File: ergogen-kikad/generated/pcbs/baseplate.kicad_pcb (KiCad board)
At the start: 2 copper layers, 73.6 x 60.5 mm, 13 parts

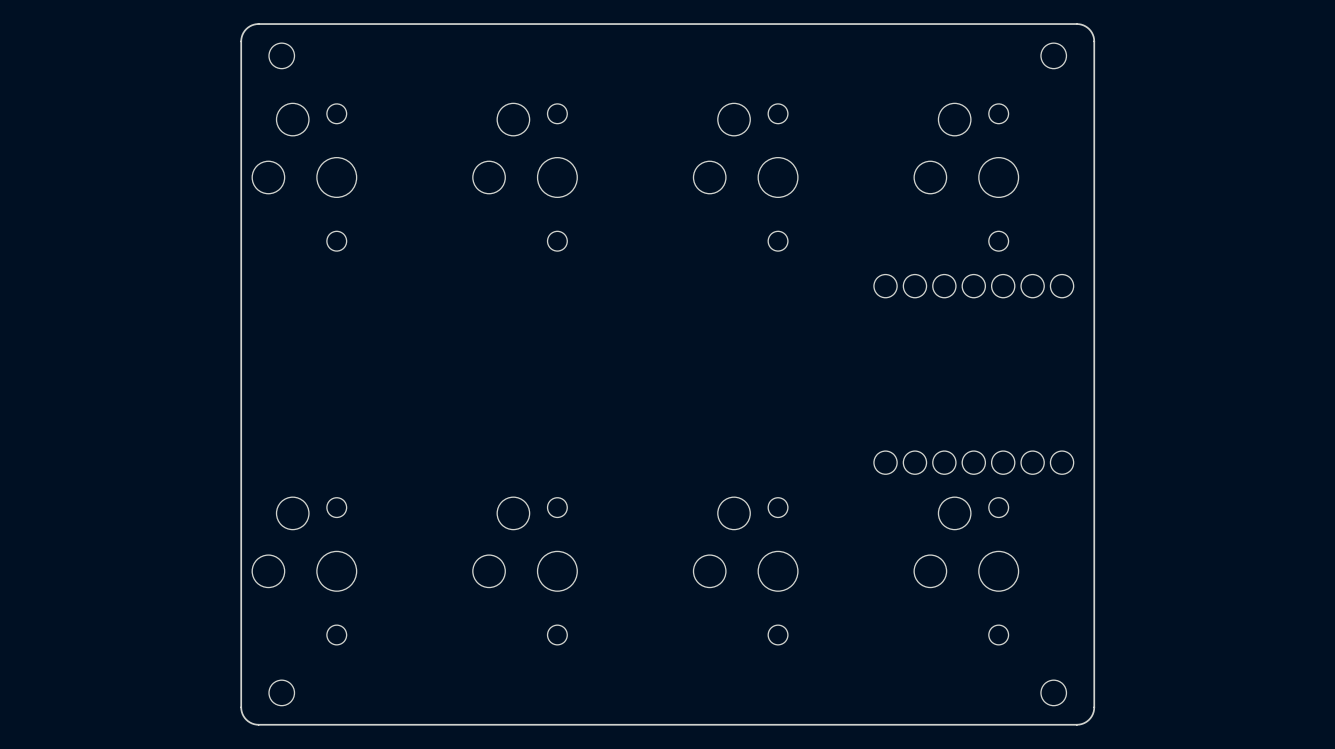
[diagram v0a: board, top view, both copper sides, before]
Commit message: Compact key rows and add controller-side keys through Ergogen
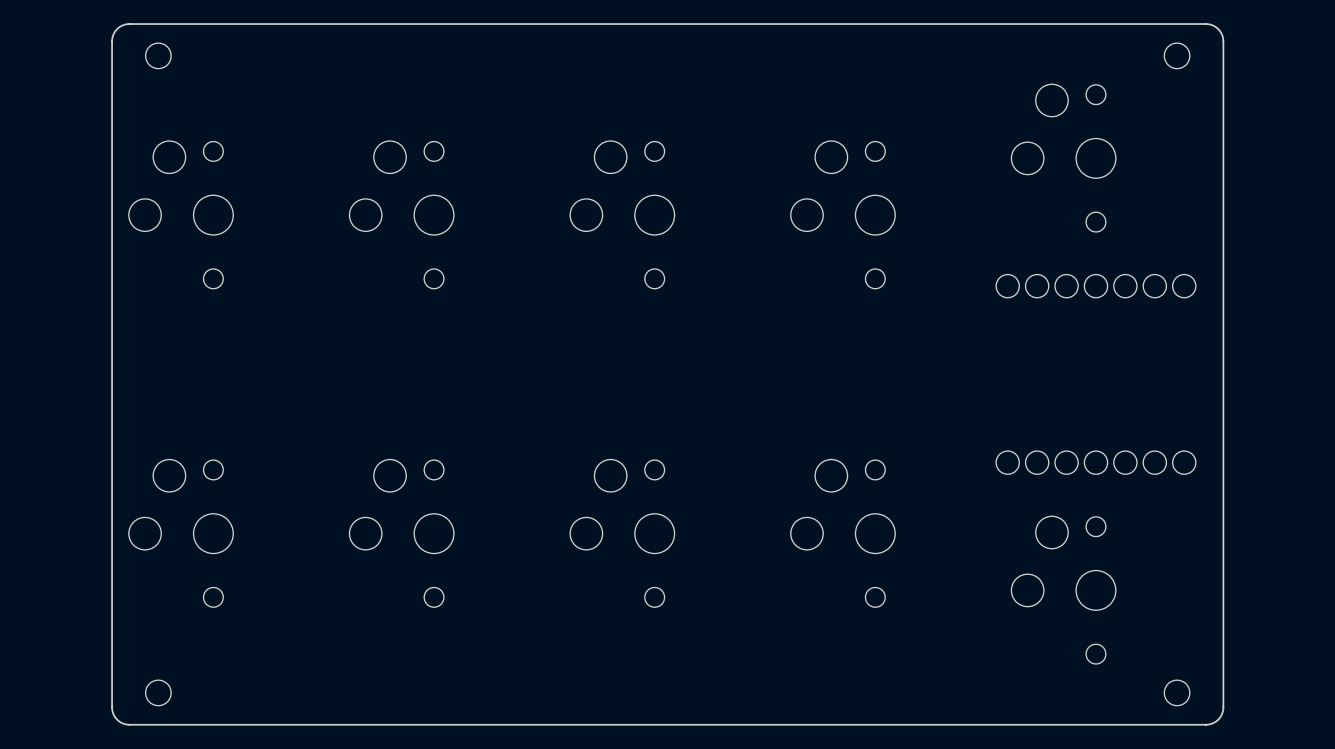
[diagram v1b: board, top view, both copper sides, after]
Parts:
- added S10: Choc v1 1U, PG1350_1U, F.Cu at (247.0, 167.2)
- added S9: Choc v1 1U, PG1350_1U, F.Cu at (247.0, 129.8)
- moved S1 11.1 mm to (170.8, 134.8)
- moved S2 11.1 mm to (189.8, 134.8)
- moved S3 11.1 mm to (208.9, 134.8)
- moved S5 11.1 mm to (170.8, 162.2)
- moved S6 11.1 mm to (189.8, 162.2)
- moved S7 11.1 mm to (208.9, 162.2)
- moved S4 11.1 mm to (227.9, 134.8)
- moved S8 11.1 mm to (227.9, 162.2)
- moved H1 10.7 mm to (166.0, 121.0)
- moved H2 10.7 mm to (254.0, 121.0)
- moved H3 10.7 mm to (166.0, 176.0)
- moved H4 10.7 mm to (254.0, 176.0)
- moved MCU1 10.5 mm to (247.0, 148.5)
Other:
- board size 73.6 x 60.5 mm -> 96 x 60.5 mm

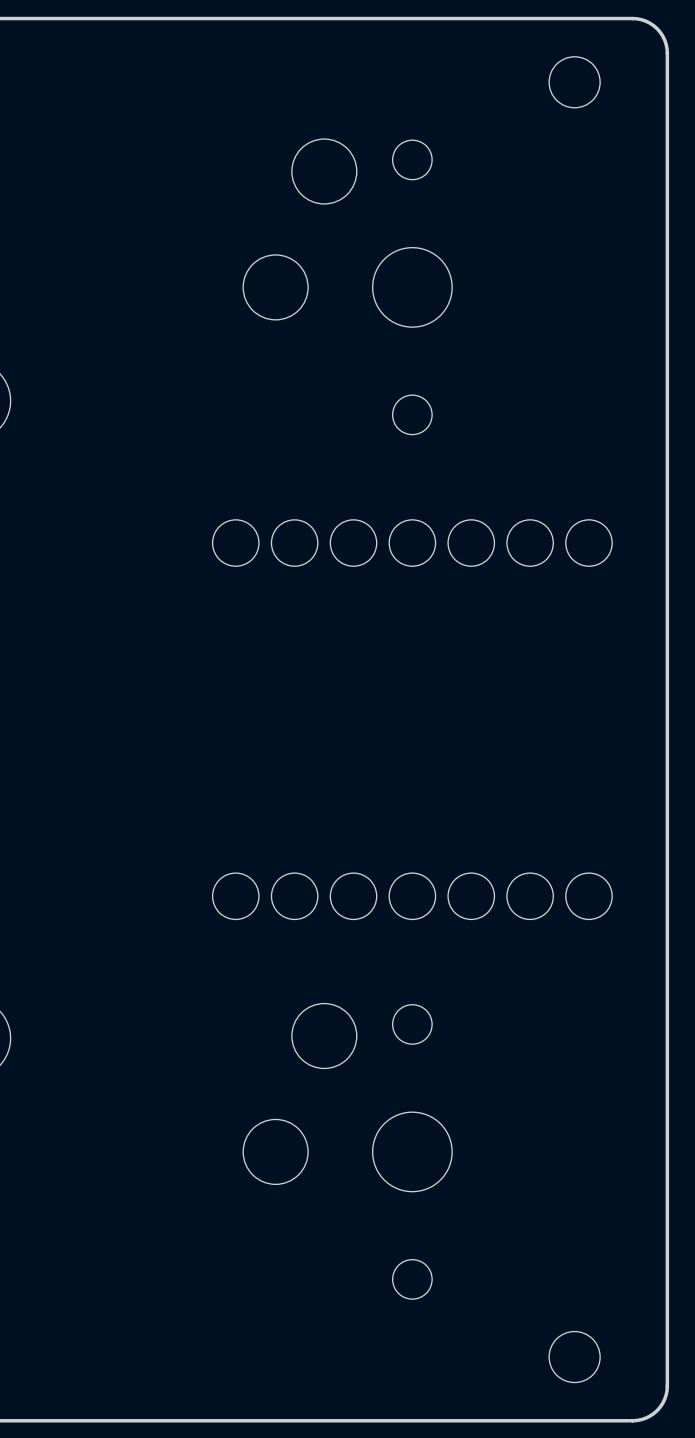
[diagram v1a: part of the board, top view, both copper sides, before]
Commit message: Align fifth-column caps with outer row edges
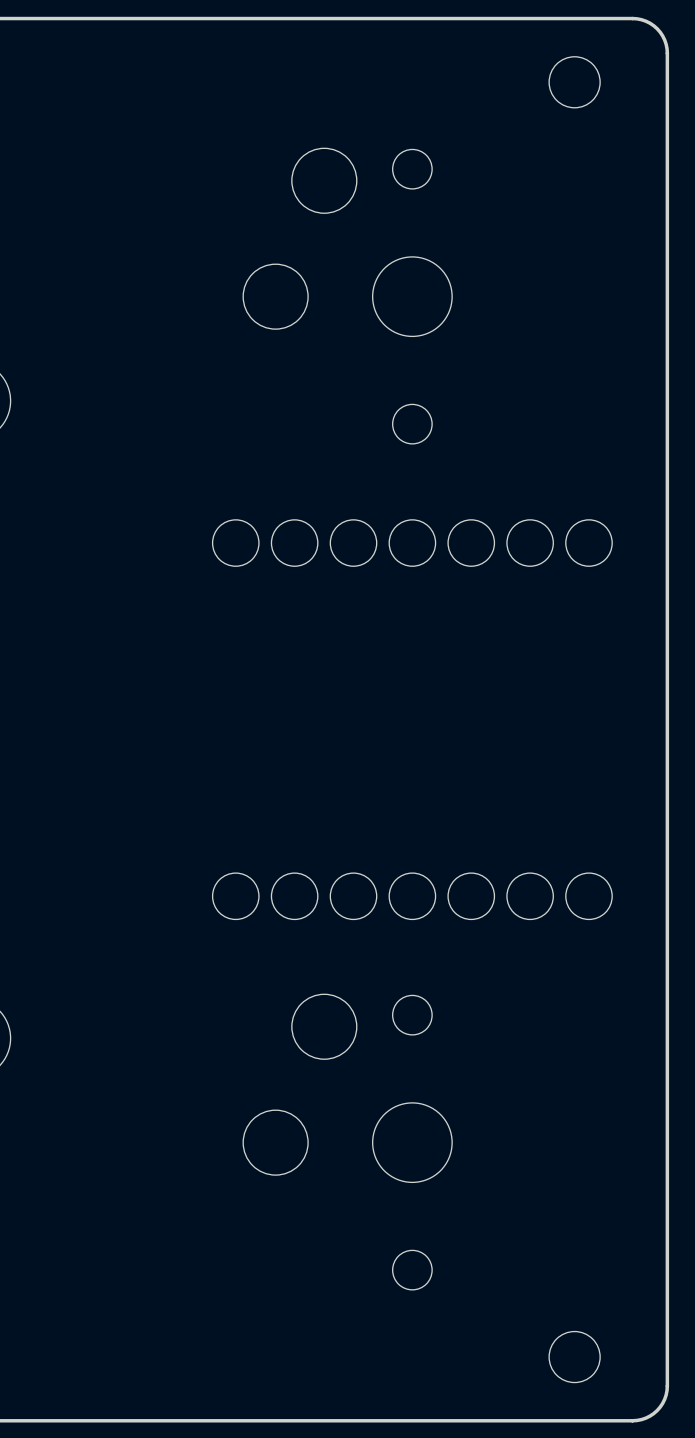
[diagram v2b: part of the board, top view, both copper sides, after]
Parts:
- moved S10 0.40 mm to (247.0, 166.8)
- moved S9 0.40 mm to (247.0, 130.2)

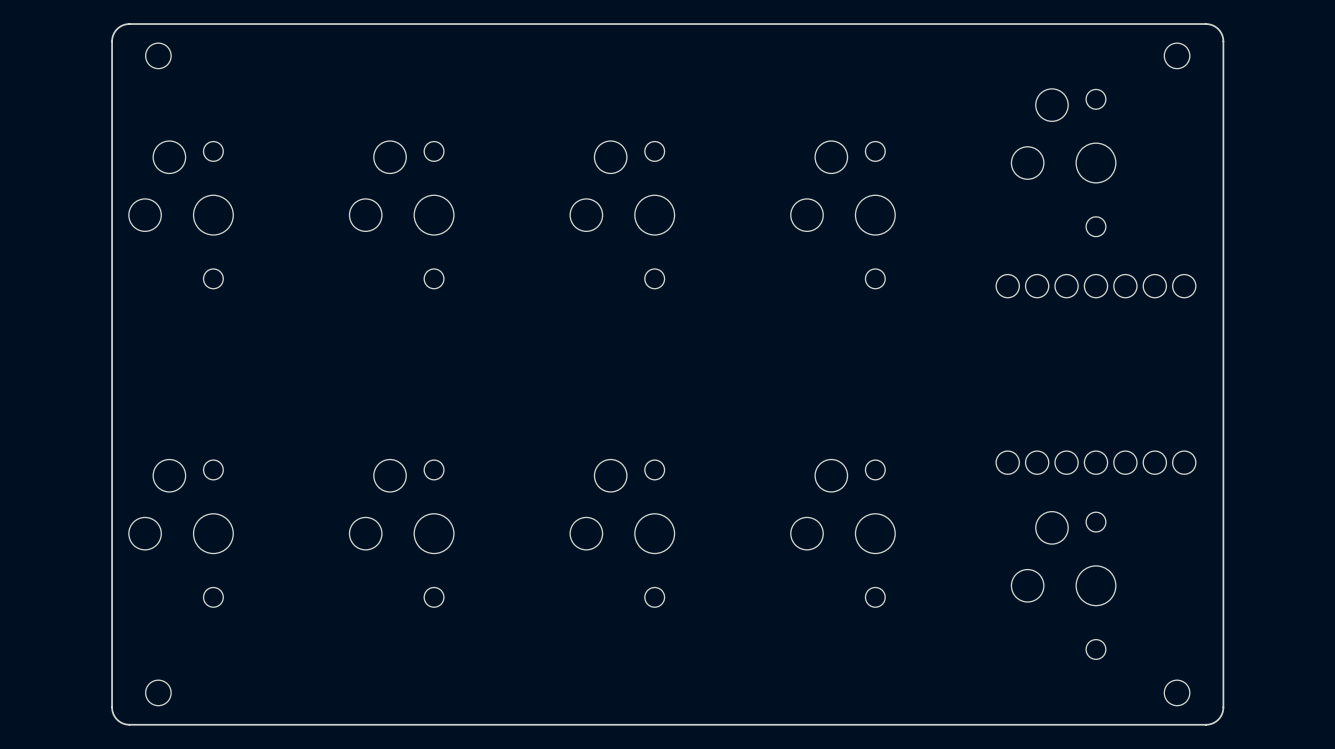
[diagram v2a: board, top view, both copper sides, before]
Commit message: Move mounts between switches and trim the board border
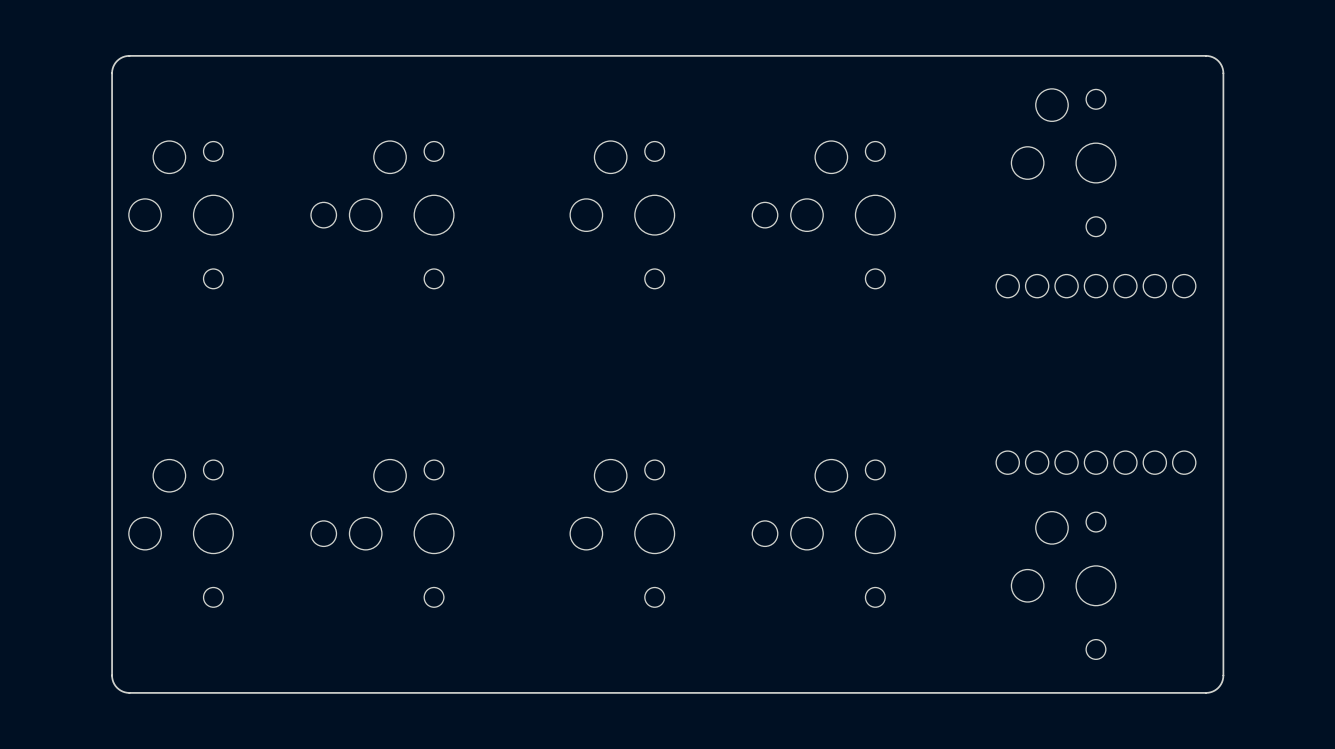
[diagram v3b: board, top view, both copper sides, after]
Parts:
- moved H2 38.1 mm to (218.4, 134.8)
- moved H4 38.1 mm to (218.4, 162.2)
- moved H1 19.8 mm to (180.3, 134.8)
- moved H3 19.8 mm to (180.3, 162.2)
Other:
- board size 96 x 60.5 mm -> 96 x 55 mm

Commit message: Add compact stacked memory LCD and regenerate matching carrier
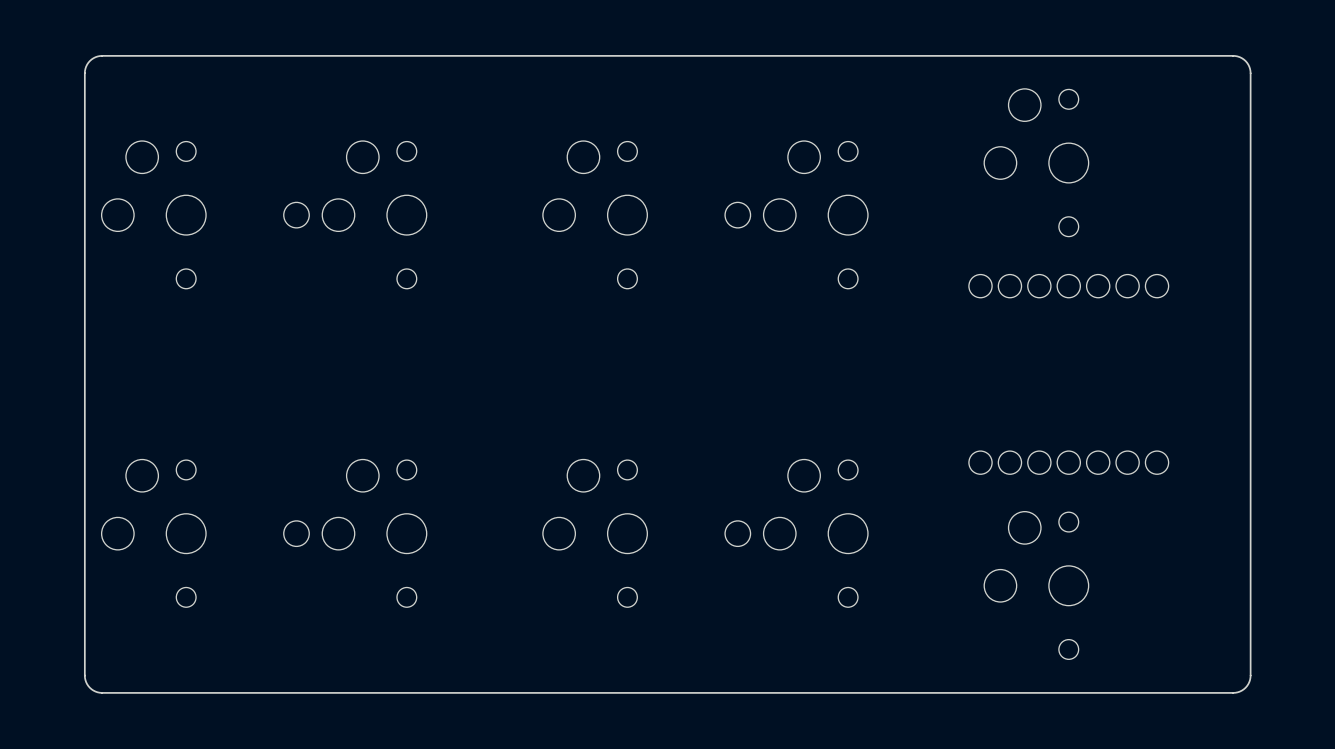
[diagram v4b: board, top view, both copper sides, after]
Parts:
- added LCD1, W1: Header clearance, , F.Cu at (168.4, 162.2)
- MCU1: value XIAO nRF52840 -> XIAO nRF52840 Plus
- moved H1 2.35 mm to (177.9, 134.8)
- moved H3 2.35 mm to (177.9, 162.2)
- moved S4 2.35 mm to (225.6, 134.8)
- moved S8 2.35 mm to (225.6, 162.2)
- moved H2 2.35 mm to (216.1, 134.8)
- moved H4 2.35 mm to (216.1, 162.2)
- moved MCU1 2.35 mm to (244.6, 148.5)
- moved S1 2.35 mm to (168.4, 134.8)
- moved S10 2.35 mm to (244.6, 166.8)
- moved S2 2.35 mm to (187.5, 134.8)
- moved S3 2.35 mm to (206.5, 134.8)
- moved S5 2.35 mm to (168.4, 162.2)
- moved S6 2.35 mm to (187.5, 162.2)
- moved S7 2.35 mm to (206.5, 162.2)
- moved S9 2.35 mm to (244.6, 130.2)
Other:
- board size 96 x 55 mm -> 100.6 x 55 mm

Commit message: Replace bare LCD with through-hole nice!view and nice!nano modules
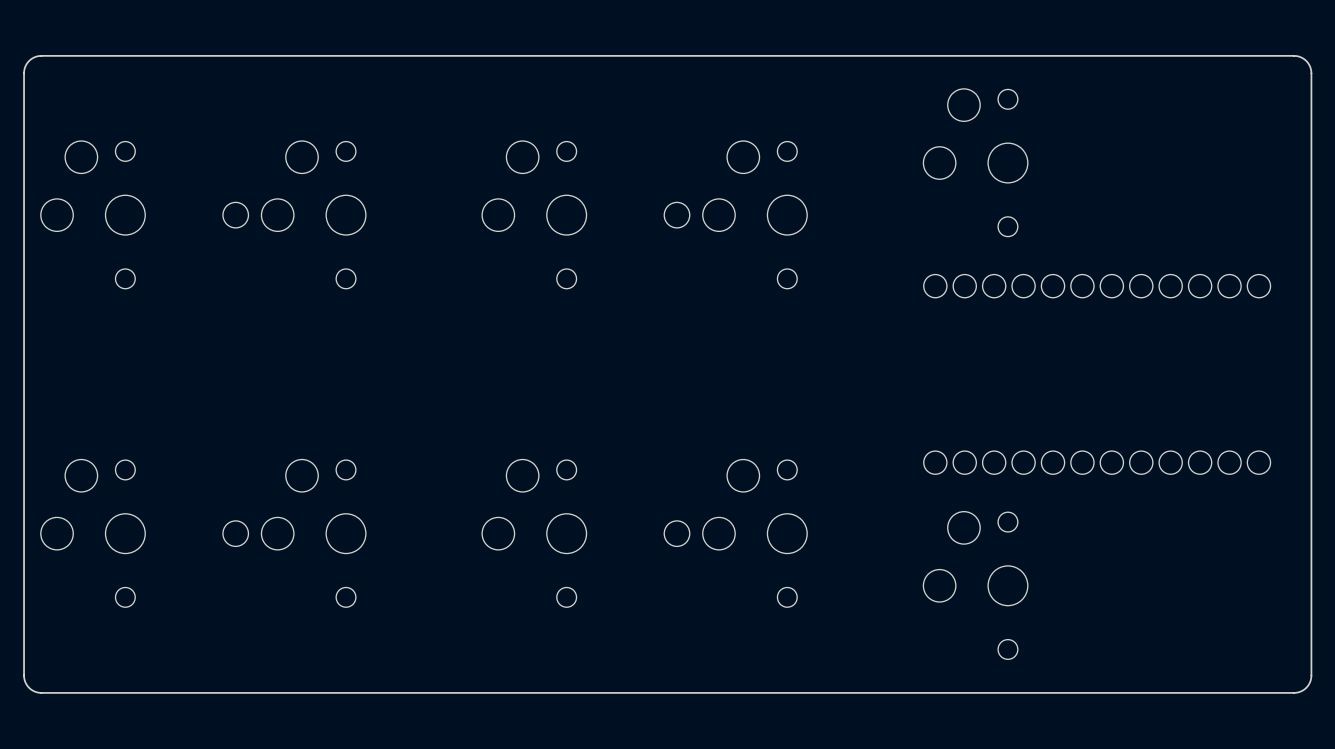
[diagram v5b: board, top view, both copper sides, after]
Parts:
- removed W1: Header clearance, 
- MCU1: value XIAO nRF52840 Plus -> nice!nano v2; footprint Seeed_XIAO_nRF52840 -> Nice_Nano_V2
- moved H1 5.25 mm to (172.7, 134.8)
- moved H2 5.25 mm to (210.8, 134.8)
- moved H3 5.25 mm to (172.7, 162.2)
- moved H4 5.25 mm to (210.8, 162.2)
- moved LCD1 5.25 mm to (163.2, 162.2)
- moved S1 5.25 mm to (163.2, 134.8)
- moved S10 5.25 mm to (239.4, 166.8)
- moved S2 5.25 mm to (182.2, 134.8)
- moved S3 5.25 mm to (201.3, 134.8)
- moved S4 5.25 mm to (220.3, 134.8)
- moved S5 5.25 mm to (163.2, 162.2)
- moved S6 5.25 mm to (182.2, 162.2)
- moved S7 5.25 mm to (201.3, 162.2)
- moved S8 5.25 mm to (220.3, 162.2)
- moved S9 5.25 mm to (239.4, 130.2)
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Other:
- board size 100.6 x 55 mm -> 111.1 x 55 mm
